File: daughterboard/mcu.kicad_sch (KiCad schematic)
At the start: 32 parts, among them J3 SWD, SW1 BOOT, SW2 RESET, U1 STM32F407VGT6, Y1 8MHz

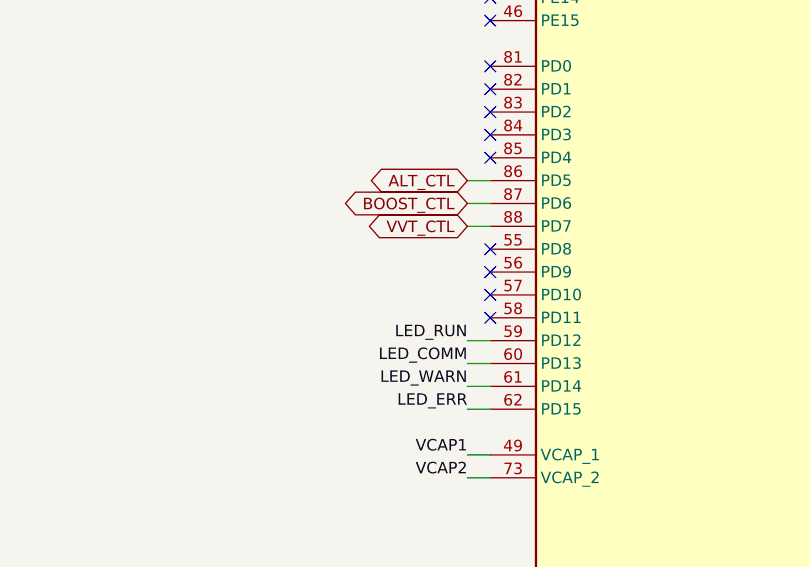
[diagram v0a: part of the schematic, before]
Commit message: IAT source jumper on every motherboard; wideband MCU flashed through the main MCU
- motherboards (1989-93 / 1994-95 rev 0.5, 1996-97 / 1999-2000 / 2001-05
  rev 0.3): the R4/R5 0R links are replaced by JP1, a 1x3 2.54 mm header with
  a removable shunt (STOCK = harness sensor, EXT = IAT connector, default)
- daughterboard rev 0.4: USART3 (PD8/PD9) to the STM32F042's ROM-bootloader
  USART1 (PA9/PA10), plus PD10 -> its BOOT0 and PD11 -> its NRST, so both
  MCUs can be flashed over the one USB-C port (rusEFI support to be written;
  SWD pads kept as a fallback)
- scripts: schematic check now also catches nets split across sheets;
  motherboard project template bundled
- README: flashing and IAT sections

Co-Authored-By: Claude Opus 5.5 <noreply@anthropic.com>
Claude-Session: https://claude.ai/code/session_012UFcA8PhPqkqYxcgEjD2n9
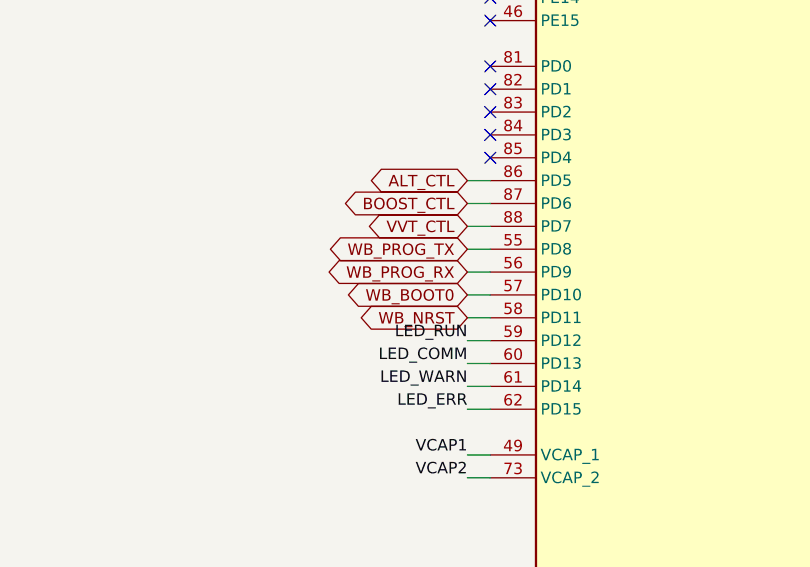
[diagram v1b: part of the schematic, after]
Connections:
- net WB_PROG_TX: now reaches U1.55 (PD8)
- net WB_PROG_RX: now reaches U1.56 (PD9)
- net WB_BOOT0: now reaches U1.57 (PD10)
- net WB_NRST: now reaches U1.58 (PD11)
- no-connect marks 32 -> 28

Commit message: Rev 0.5 daughterboard, rev 0.6 1989-93/1994-95 motherboards: review fixes
Daughterboard rev 0.5:
- SN74LVC4245A drives the eight AUIPS2041 low sides at 5 V; output enable pulled
  off (R71) until the firmware enables it on PA8.
- BOOT1 pull-down (R72); hall input clamps D13/D14.
- ULN2003 COM to an SMAJ33A TVS (D11) instead of +12V: no key-off back-feed,
  no conduction in a 35 V load dump.
- Logic supply: D7/D8 -> 0.5 A PTC F1 -> SMAJ33A D12; C16 50 V, SS36 D9, C59.
- Tach stays an output.

Motherboards:
- Idle/VVT freewheel diodes, 4.7k switch pull-up options (not fitted),
  AUX VBAT PTC on all years.
- 1989-93 rev 0.6: two drivers per injector wire (0R links), SMCJ40A clamps.
- 2001-05: J1 3B tied to 3A.

Firmware: low-side enable (inverted open drain, forced writes, off during
configuration changes), unused control pins parked with pull-down, 1989-93
batch on all four outputs, VBATT offset noted.

Verification: 18/18 board tests, 119/119 harness check, circuit sims
20 OK / 3 CHECK / 6 REF / 0 FAIL, flash sim 9/9, firmware and bootloader
build; all boards 0 unconnected, 0 clearance errors.

Co-Authored-By: Claude Opus 5.5 <noreply@anthropic.com>
Claude-Session: https://claude.ai/code/session_012UFcA8PhPqkqYxcgEjD2n9
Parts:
- added R72: 10k, Resistor_SMD:R_0402_1005Metric, symbol Device:R
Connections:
- net GND: now also R72.2
- net BOOT1: now reaches U1.37 (PB2)
- net BOOT1: now also R72.1
- net DRV_EN_N: now reaches U1.67 (PA8)
- no-connect marks 28 -> 26
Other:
- note added: "BOOT1 (PB2) low: DFU needs BOOT0 = 1, BOOT1 = 0"

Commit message: Daughterboard: 5.5 A buck inductor, 33 pF crystal caps; NB alternator control off by default
- L2: Sunlord MWSA0603S-100MT (C132141, 10 uH, Isat 5.5 A, 7 x 6.6 mm). The
  MWSA0503S saturated at 3.5 A, below the LMR14020's 3.8 A maximum current
  limit. Placed on end; D9 and the feedback divider moved 0.3 mm left.
- C13/C14: 33 pF C0G (C1663) for the 20 pF crystal (were 22 pF).
- Firmware: NB alternator control ships off until the field current is
  measured (pin, PID and target still set up). Test checks the field isn't
  driven with the default tune.
- Daughterboard re-routed and released: 754 pads match, 0 unconnected,
  0 clearance errors. Viewer assets and README renders refreshed.

Co-Authored-By: Claude Opus 5.5 <noreply@anthropic.com>
Claude-Session: https://claude.ai/code/session_012UFcA8PhPqkqYxcgEjD2n9
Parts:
- C13, C14: value 22p -> 33p; LCSC C1653 -> C1663

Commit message: Daughterboard rev 0.5b: in-stock parts for JLCPCB assembly
JLCPCB's BOM check flagged ten lines short of stock and one footprint mismatch.
All replacements are in stock at JLCPCB and fit the existing footprints (no re-route):
- Q1-Q8: onsemi NCV8406ASTT3G (C459816) instead of AUIPS2041LTR: same SOT-223
  pinout, 60-70 V active clamp, current limit, thermal shutdown, AEC-Q101.
- D11/D12 Littelfuse SMAJ33A (C223988); F1 TECHFUSE nSMD050-33V (C70077);
  L1 FH CMI322513U2R2KT (C70960); LEDs KENTO KT-0603G/B/Y; C103 YAGEO 33 nF
  50 V (C106862); R110 62 ohm 1% (C23222, was 61.9).
- U9 (MAX9926, spare VR inputs, out of stock everywhere) not fitted.
- U105 footprint renamed SOT-23-5 (AD8628ARTZ; pads identical to TSOT-23-5).
- JLC BOM: one line per LCSC part (SW1/SW2); not-fitted parts excluded.

Re-checked: netlist 754 pads 0 differences, DRC 0 unconnected / 0 clearance,
circuit sims with the NCV8406A model 20 OK / 3 CHECK / 6 REF / 0 FAIL.

Co-Authored-By: Claude Opus 5.5 <noreply@anthropic.com>
Claude-Session: https://claude.ai/code/session_012UFcA8PhPqkqYxcgEjD2n9
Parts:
- D1, D5: LCSC C72043 -> C12624
- D2: LCSC C72041 -> C2288
- D3: LCSC C72038 -> C2287
